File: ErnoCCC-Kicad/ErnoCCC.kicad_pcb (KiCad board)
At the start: 2 copper layers, 161.4 x 95.9 mm, 106 parts, among them J1 6VAC, J2 ICSP, J3 FTDI, J4 Erno Controller, J5 SWITCH, J6 LED OUT, J7 Conn_01x07, Q1 BC847, Q2 BC847, Q3 BC847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

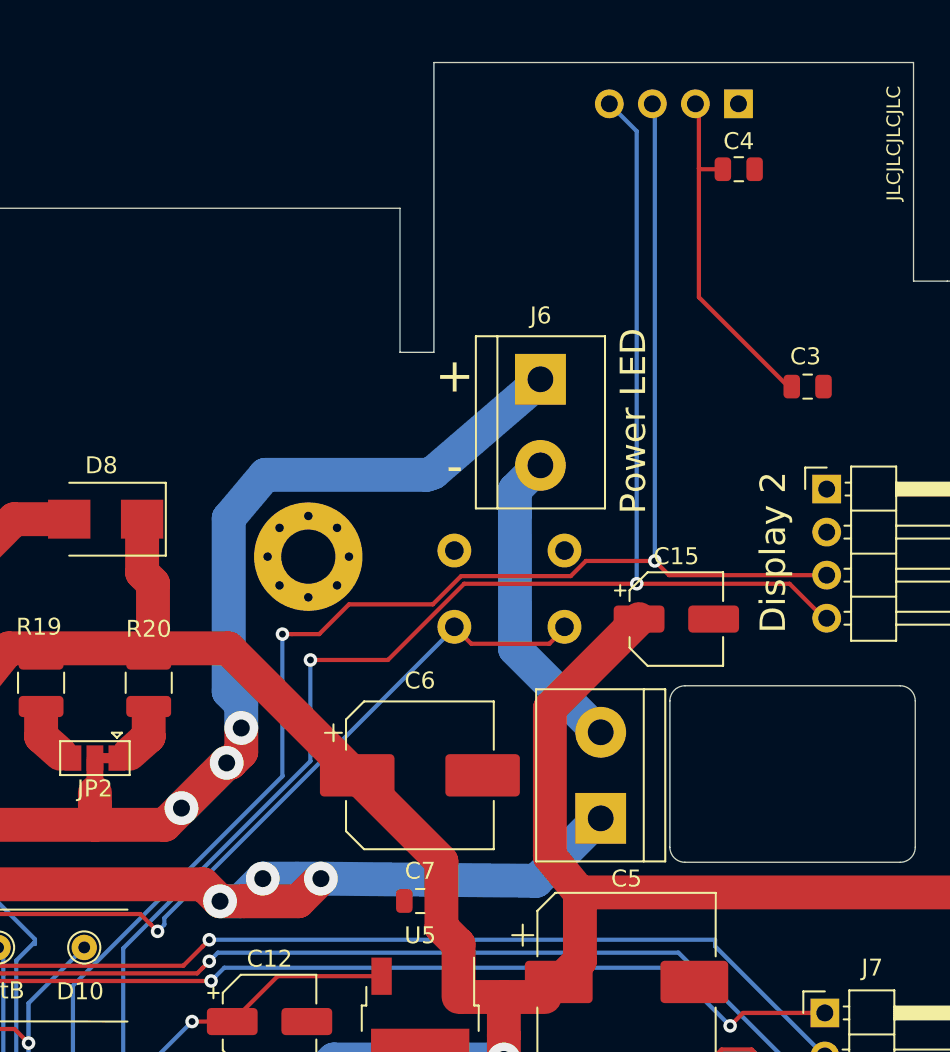
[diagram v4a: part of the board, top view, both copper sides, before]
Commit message: Fixing i2c bus, making OLED polarity conifgurable, submitting final ReV gerbers
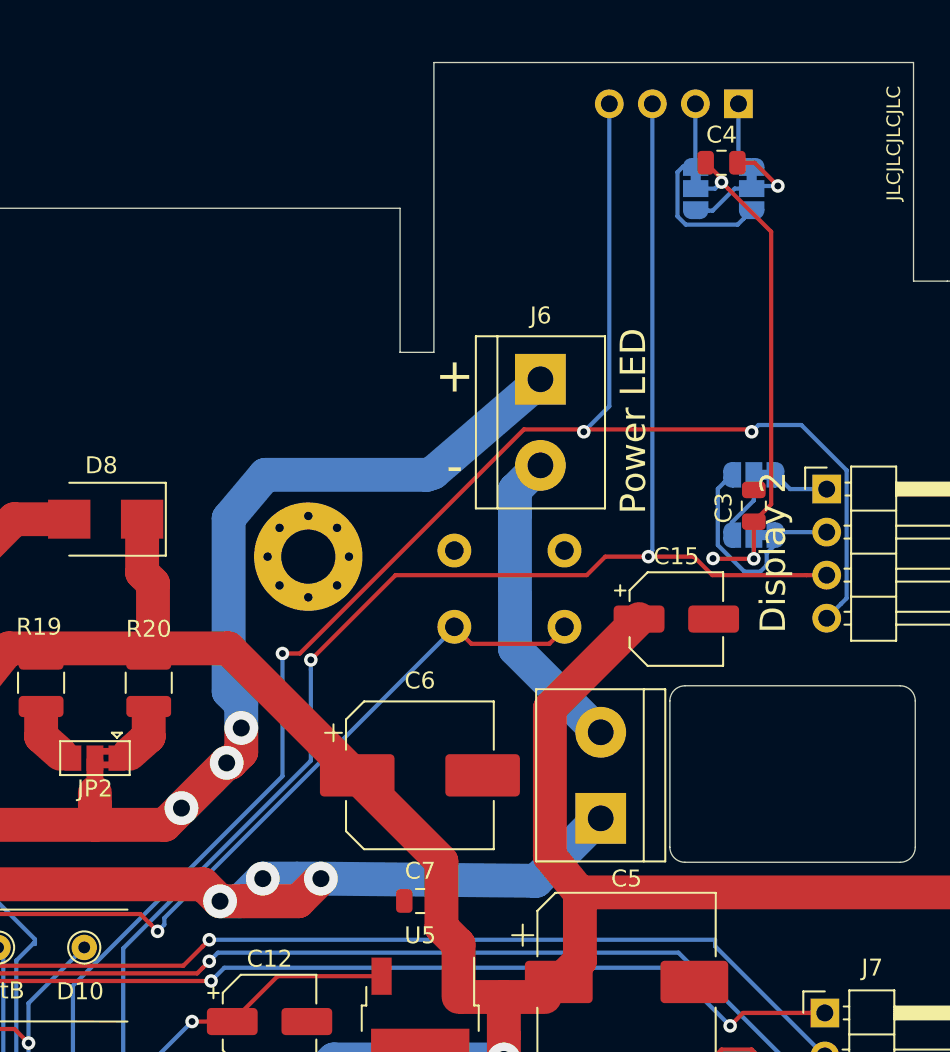
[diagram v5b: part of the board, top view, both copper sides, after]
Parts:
- added JP3: VCC Ctrl, Jumper:SolderJumper-3_P1.3mm_Bridged12_RoundedPad1.0x1.5mm, B.Cu at (209.7, 53.1)
- added JP4: GND Ctrl, Jumper:SolderJumper-3_P1.3mm_Bridged12_RoundedPad1.0x1.5mm, B.Cu at (209.7, 49.5)
- added JP5: VCC Ctrl, Jumper:SolderJumper-3_P1.3mm_Bridged12_RoundedPad1.0x1.5mm, B.Cu at (206.2, 32.6)
- added JP6: GND Ctrl, Jumper:SolderJumper-3_P1.3mm_Bridged12_RoundedPad1.0x1.5mm, B.Cu at (209.6, 32.6)
- JP2: footprint Jumper:SolderJumper-3_P1.3mm_Bridged12_Pad1.0x1.5mm -> Jumper:SolderJumper-3_P1.3mm_Bridged2Bar12_Pad1.0x1.5mm
- R10, R9: value 10k -> 2k2
- moved C3 7.72 mm to (209.7, 51.4), turned to 90 degrees
- moved C4 1.09 mm to (207.8, 31.1)
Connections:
- D7 pad 1: GND -> Net-(D7-Pad1)
- D7 pad 2: +5V -> Net-(D7-Pad2)
- D7 pad 3: /SDA -> /SCL
- D7 pad 4: /SCL -> /SDA
- D9 pad 1: GND -> Net-(D9-Pad1)
- D9 pad 2: +5V -> Net-(D9-Pad2)
- D9 pad 3: /SDA -> /SCL
- D9 pad 4: /SCL -> /SDA
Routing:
- net Net-(D9-Pad2): track 0.00 -> 13.3 mm
- net GND: track 163.5 -> 176.0 mm, vias 12 -> 13
- net Net-(D7-Pad2): track 0.00 -> 12.5 mm
- net +5V: track 108.5 -> 118.7 mm, vias 13 -> 16
- net /SDA: track 128.5 -> 135.3 mm, vias 3 -> 4
- net Net-(D7-Pad1): track 0.00 -> 4.03 mm
- net Net-(D9-Pad1): track 0.00 -> 3.35 mm
- net /SCL: track 128.8 -> 126.6 mm

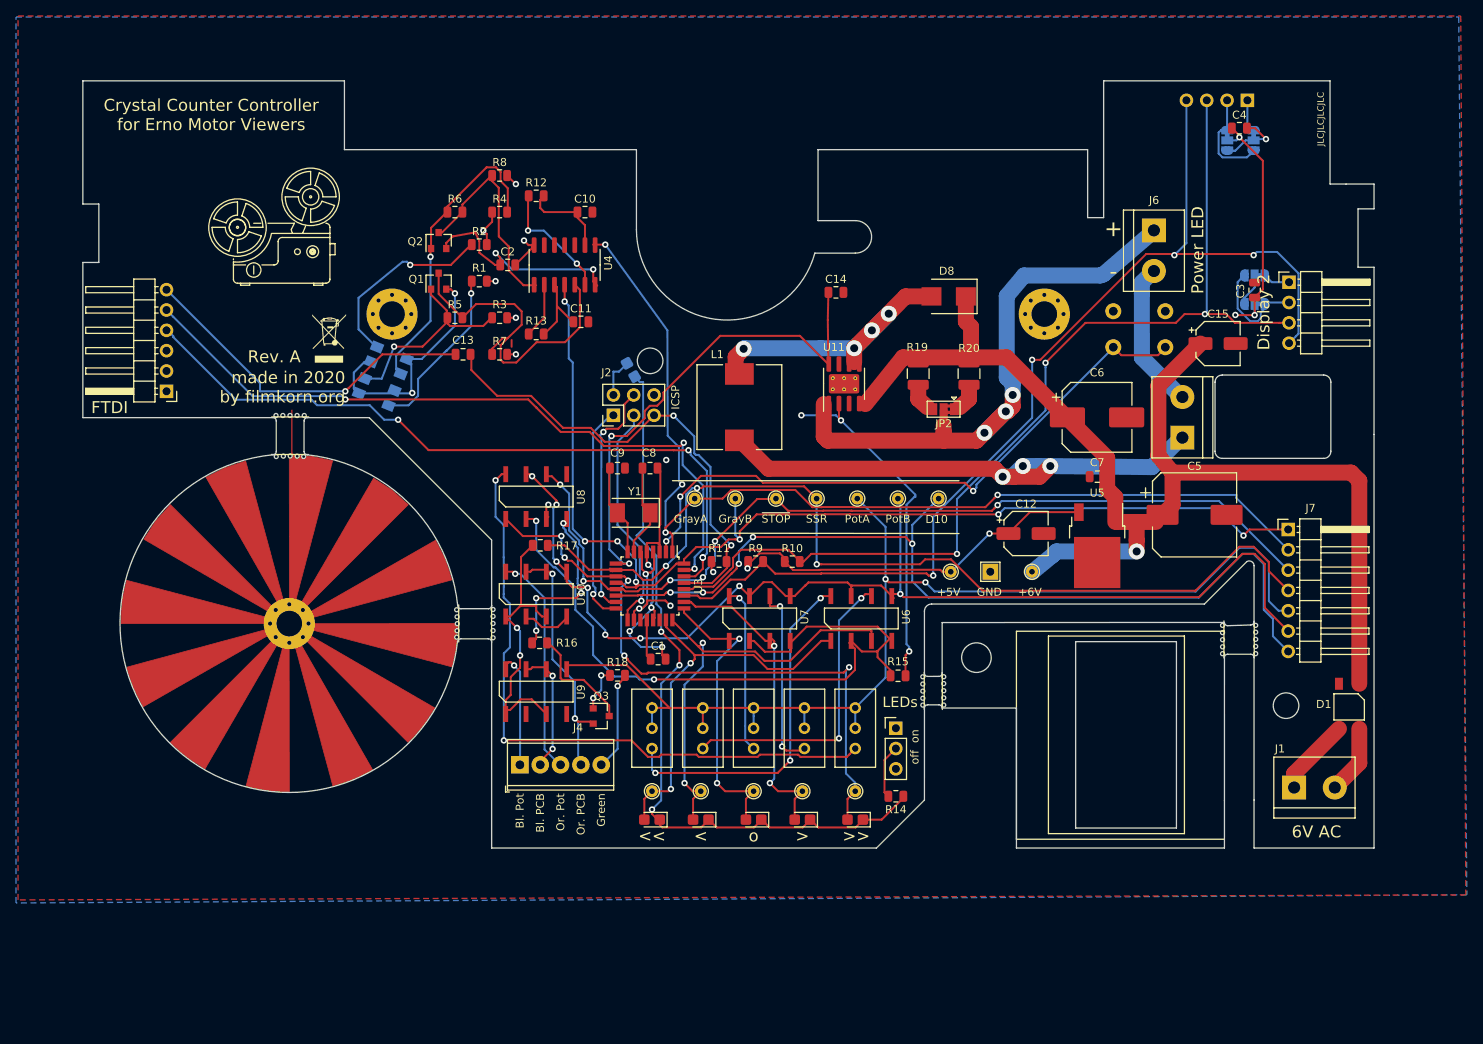
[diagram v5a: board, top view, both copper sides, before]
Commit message: Preparing for the big refactoring (old footprints still there)
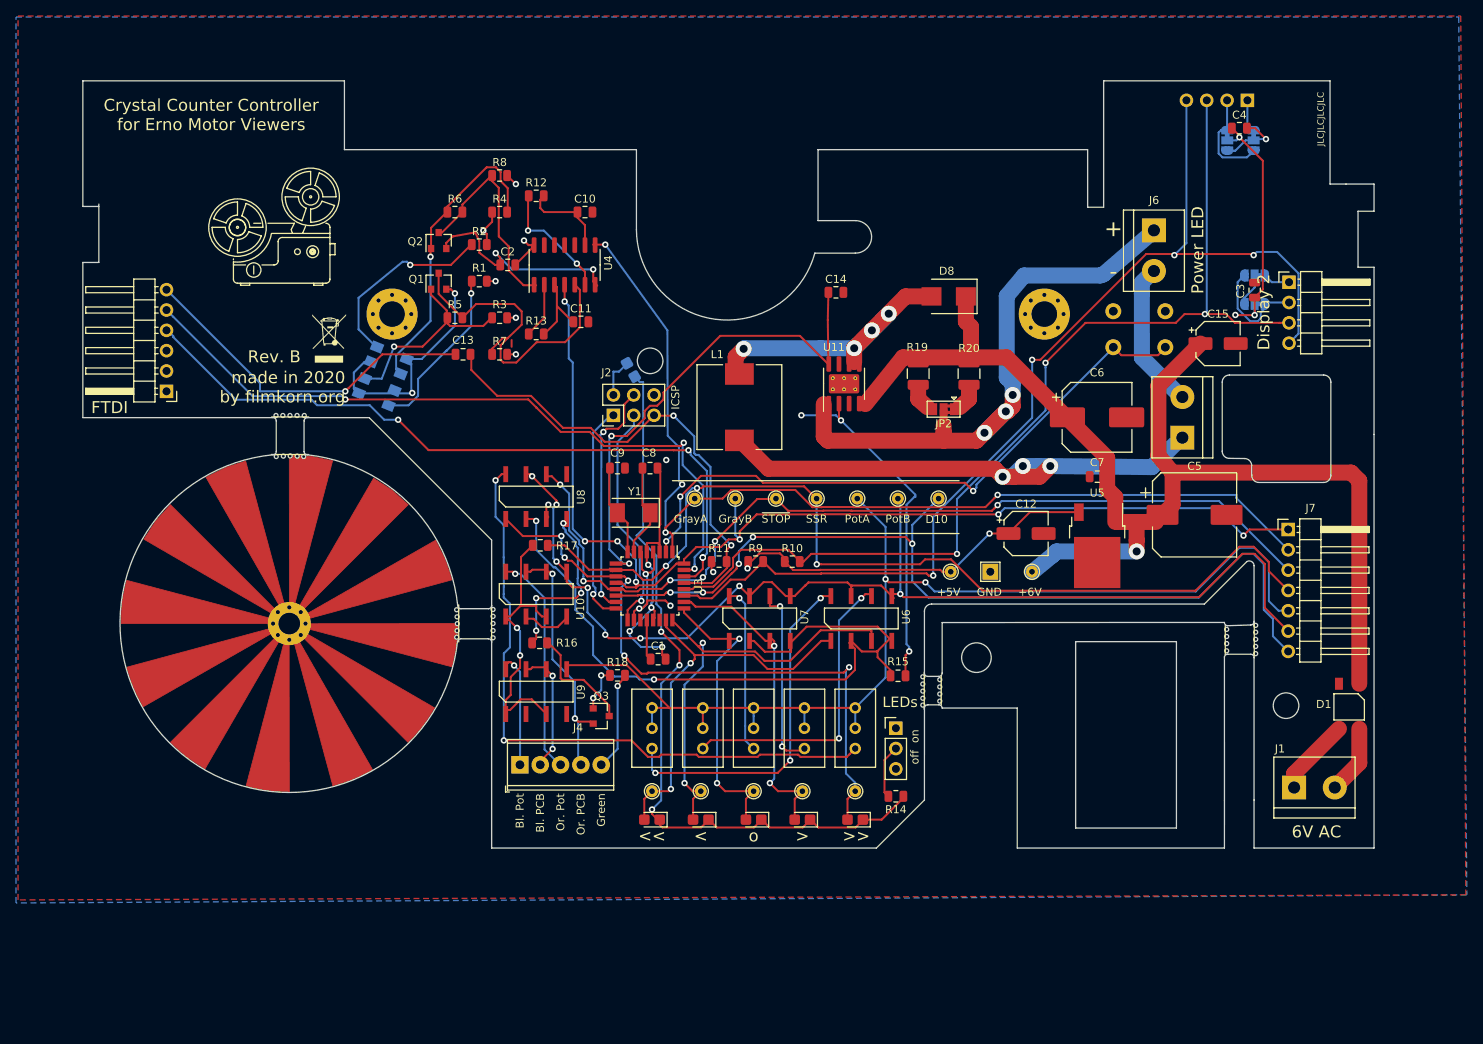
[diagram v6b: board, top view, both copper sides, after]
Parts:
- REF**: value MountingHole_3.2mm_M3_Pad_Via -> MountingHole_2.7mm_Pad_Via; footprint MountingHole:MountingHole_3.2mm_M3_Pad_Via -> MountingHole:MountingHole_2.7mm_Pad_Via
- REF** (x2): footprint ErnoCCC:MouseBites5x1 -> ErnoCCC:MouseBites4x1
- REF** (x5): value Mouse Bites 4x1 -> Mouse Bites 5x1
- REF**: value Mouse Bites 4x1 -> Mouse Bites 5x1 curved
- moved REF** 3.26 mm to (172.2, 101.4), turned to 90 degrees
- moved REF** 3.24 mm to (204.3, 95.1), turned to 270 degrees
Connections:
- J7 pad 5: /POTA -> (no net)
- J7 pad 6: /POTB -> (no net)
- U3 pad 19: Net-(U3-Pad19) -> (no net)
- U3 pad 22: Net-(U3-Pad22) -> (no net)
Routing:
- net (no net): track 0.85 -> 162.6 mm, vias 0 -> 3
- net /POTA: track 142.1 -> 48.6 mm, vias 2 -> 0
- net /POTB: track 139.5 -> 68.6 mm, vias 8 -> 7
- net GND: track 176.0 -> 155.4 mm
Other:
- outline, holes or cut-outs redrawn
- board text added: "Cut/Shorten both Jumpers to swap Display ploarity"
- board text added: "Rev. B"
- board text removed: "Rev. A"

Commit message: Preparing for the big RevB rerouting
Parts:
- removed Q3: BC847, Package_TO_SOT_SMD:SOT-23
- removed the REF** at (94.0, 57.4)
- removed RV2, RV3, RV4, RV5: 4k7, Potentiometer_THT:Potentiometer_Bourns_3296W_Vertical
- removed TP10: >, TestPoint:TestPoint_THTPad_D1.5mm_Drill0.7mm
- removed TP11: >>, TestPoint:TestPoint_THTPad_D1.5mm_Drill0.7mm
- removed TP12: ~STOP~, TestPoint:TestPoint_THTPad_D1.5mm_Drill0.7mm
- removed TP13: PotA, TestPoint:TestPoint_THTPad_D1.5mm_Drill0.7mm
- removed TP14: PotB, TestPoint:TestPoint_THTPad_D1.5mm_Drill0.7mm
- removed TP6: SSR, TestPoint:TestPoint_THTPad_D1.5mm_Drill0.7mm
- removed TP7: <<, TestPoint:TestPoint_THTPad_D1.5mm_Drill0.7mm
- removed TP8: <, TestPoint:TestPoint_THTPad_D1.5mm_Drill0.7mm
- removed TP9: o, TestPoint:TestPoint_THTPad_D1.5mm_Drill0.7mm
- removed U8: CPC2017N, ErnoCCC:SOIC-8
- added C16: 100n, Capacitor_SMD:C_0805_2012Metric, F.Cu at (93.7, 134.1)
- added C17: 1u, Capacitor_SMD:C_0805_2012Metric, F.Cu at (88.2, 142.8)
- J4: footprint TerminalBlock_Phoenix:TerminalBlock_Phoenix_MPT-0,5-5-2.54_1x05_P2.54mm_Horizontal -> TerminalBlock_Phoenix:TerminalBlock_Phoenix_MPT-0,5-7-2.54_1x07_P2.54mm_Horizontal
- J7: value Conn_01x07 -> Conn_01x05; footprint Connector_PinHeader_2.54mm:PinHeader_1x07_P2.54mm_Horizontal -> Connector_PinHeader_2.54mm:PinHeader_1x05_P2.54mm_Horizontal
- R15: value 1k5 -> 27k
- R16: value 1k5 -> 5k6
- R17: value 330 -> 470
- R18: value 10k -> 47k
- U6: value CPC2017N -> NCS20071; footprint ErnoCCC:SOIC-8 -> Package_TO_SOT_SMD:TSOT-23-5
- U7: value CPC2017N -> MCP4725; footprint ErnoCCC:SOIC-8 -> Package_TO_SOT_SMD:SOT-23-6
- moved R15 96.9 mm to (77.6, 141.2), turned to 0 degrees
- moved U6 85.7 mm to (88.7, 139.1)
- moved U7 71.4 mm to (93.8, 139.2)
- moved R18 62.7 mm to (83.2, 141.2)
- moved RV1 60.7 mm to (82.9, 135.9), turned to 0 degrees
- moved R16 50.4 mm to (88.7, 134.7), turned to 0 degrees
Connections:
- J4 pad 1: Net-(J4-Pad1) -> +15V
- J7 pad 3: /~STOP~ -> /SSR
- J7 pad 4: /SSR -> /D9
- J7 pad 5: (no net) -> /D10
- R15 pad 1: GND -> Net-(R15-Pad1)
- R16 pad 1: Net-(Q3-Pad3) -> Net-(R16-Pad1)
- R16 pad 2: Net-(R16-Pad2) -> /DAC
- R18 pad 1: Net-(Q3-Pad1) -> /VCTRL
- R18 pad 2: Net-(J4-Pad5) -> Net-(R15-Pad2)
- RV1 pad 1: /POTA -> GND
- RV1 pad 2: /POTA -> GND
- RV1 pad 3: Net-(RV1-Pad3) -> Net-(R15-Pad1)
- U10 pad 5: /POTB -> Net-(U10-Pad5)
- U10 pad 6: Net-(J4-Pad4) -> Net-(U10-Pad6)
- U10 pad 7: Net-(J4-Pad4) -> Net-(J4-Pad6)
- U10 pad 8: Net-(J4-Pad3) -> Net-(J4-Pad5)
- U3 pad 13: /~STOP~ -> /D9
- U3 pad 19: (no net) -> Net-(U3-Pad19)
- U3 pad 22: (no net) -> Net-(U3-Pad22)
- U6 pad 1: /<< -> /VCTRL
- U6 pad 2: Net-(R15-Pad2) -> GND
- U6 pad 3: /< -> Net-(R16-Pad1)
- U6 pad 5: /POTB -> +15V
- U7 pad 1: /o -> /VCTRL
- U7 pad 2: Net-(R15-Pad2) -> GND
- U7 pad 3: /> -> +5V
- U7 pad 4: Net-(R15-Pad2) -> Net-(U7-Pad4)
- U7 pad 5: /POTB -> Net-(U7-Pad5)
- U7 pad 6: Net-(RV4-Pad3) -> GND
- U9 pad 5: /POTA -> /VCTRL
- U9 pad 6: Net-(J4-Pad2) -> Net-(J4-Pad4)
- U9 pad 7: Net-(J4-Pad2) -> Net-(J4-Pad3)
- U9 pad 8: Net-(J4-Pad1) -> Net-(J4-Pad2)
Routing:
- net (no net): track 162.6 -> 0.85 mm, vias 3 -> 0
- net /SSR: track 119.2 -> 0.00 mm, vias 3 -> 0
- net /~STOP~: track 115.1 -> 0.00 mm, vias 6 -> 0
- net Net-(D10-Pad1): track 96.3 -> 0.00 mm, vias 3 -> 0
- net Net-(R15-Pad2): track 89.6 -> 0.00 mm, vias 2 -> 0
- net Net-(RV5-Pad3): track 80.8 -> 0.00 mm, vias 2 -> 0
- net />>: track 78.9 -> 0.00 mm, vias 5 -> 0
- net /POTB: track 68.6 -> 0.00 mm, vias 7 -> 0
- net /D9: track 0.00 -> 66.2 mm, vias 0 -> 1
- net /<: track 55.1 -> 0.00 mm, vias 2 -> 0
- net GND: track 155.4 -> 102.3 mm, vias 13 -> 9
- net /<<: track 49.3 -> 0.00 mm, vias 2 -> 0
- net /POTA: track 48.6 -> 0.00 mm
- net Net-(RV1-Pad3): track 44.2 -> 0.00 mm, vias 3 -> 0
- net />: track 39.2 -> 0.00 mm, vias 2 -> 0
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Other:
- board text removed: "PotA"
- board text removed: "PotB"
- board text removed: "~STOP"
